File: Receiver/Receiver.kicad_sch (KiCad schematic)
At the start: 2 parts, among them J1 Conn_01x03, U1 TSSP4038

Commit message: gnd fills
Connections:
- net GND: now reaches J1.3 (Pin_3), U1.2
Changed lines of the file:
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@@
 	(generator_version "8.0")
 	(paper "A4")
+	(junction
+		(at 124.46 96.52)
+		(diameter 0)
+		(color 0 0 0 0)
+	)
 	(wire
 		(pts
@@
 					(unit 1)
 				)
+			)
+		)
+	)
+	(symbol
+		(lib_id "power:GND")
+		(at 124.46 96.52 0)
+		(unit 1)
+		(exclude_from_sim no)
+		(in_bom yes)
+		(on_board yes)
+		(dnp no)
+		(fields_autoplaced yes)
+		(property "Reference" "#PWR01"
+			(at 124.46 102.87 0)
+			(effects
+				(font
+					(size 1.27 1.27)
+				)
+				(hide yes)
+			)
+		)
+		(property "Value" "GND"
+			(at 124.46 101.6 0)
+			(effects
+				(font
+					(size 1.27 1.27)
+				)
+			)
+		)
+		(property "Footprint" ""
+			(at 124.46 96.52 0)
+			(effects
+				(font
+					(size 1.27 1.27)
+				)
+				(hide yes)
+			)
+		)
+		(property "Datasheet" ""
+			(at 124.46 96.52 0)
+			(effects
+				(font
+					(size 1.27 1.27)
+				)
+				(hide yes)
+			)
+		)
+		(property "Description" "Power symbol creates a global label with name \"GND\" , ground"
+			(at 124.46 96.52 0)
+			(effects
+				(font
+					(size 1.27 1.27)
+				)
+				(hide yes)
+			)
+		)
+		(pin "1"
+		)
+		(instances
+			(project "Receiver"
+				(path "/7e0fe819-ccc9-4312-883b-b9dcc40b4756"
+					(reference "#PWR01")
+					(unit 1)
+				)

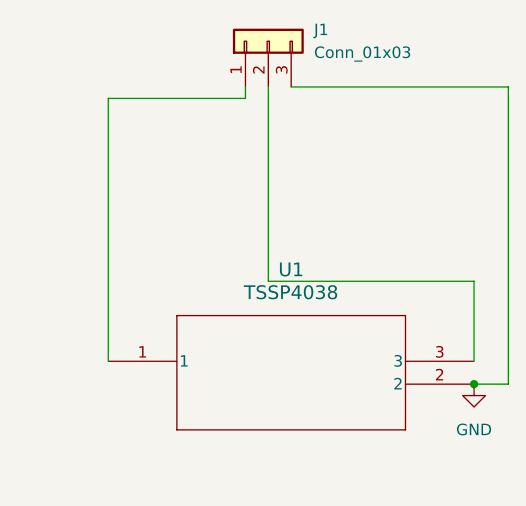
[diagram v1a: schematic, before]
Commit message: Added low pass filter to reciever pcb
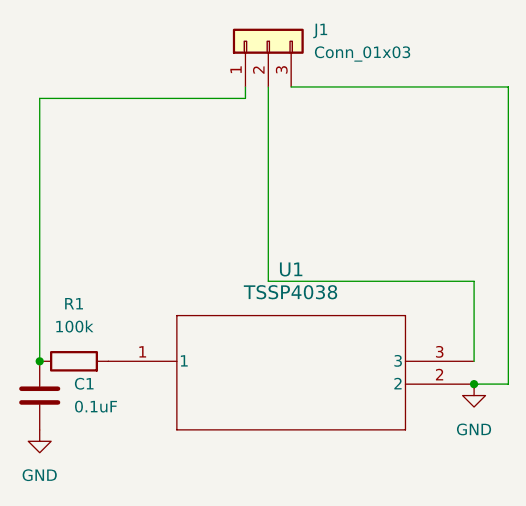
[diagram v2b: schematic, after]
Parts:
- added C1: 0.1uF, Capacitor_SMD:C_0805_2012Metric_Pad1.18x1.45mm_HandSolder, symbol Device:C
- added R1: 100k, Resistor_SMD:R_0805_2012Metric_Pad1.20x1.40mm_HandSolder, symbol Device:R
- J1: footprint Connector_JST:JST_XH_S3B-XH-A-1_1x03_P2.50mm_Horizontal -> Connector_JST:JST_XH_B3B-XH-AM_1x03_P2.50mm_Vertical
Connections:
- net GND: now also C1.2
- net at J1.1 (Pin_1): now also C1.1, R1.1; no longer U1.1
- new net: R1.2, U1.1
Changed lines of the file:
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@@
 	(paper "A4")
+	(junction
+		(at 76.2 93.98)
+		(diameter 0)
+		(color 0 0 0 0)
+	)
 	(junction
 		(at 124.46 96.52)
@@
 	(wire
 		(pts
-			(xy 83.82 64.77) (xy 83.82 93.98)
+			(xy 76.2 93.98) (xy 76.2 64.77)
 		)
 		(stroke
@@
 	(wire
 		(pts
-			(xy 99.06 64.77) (xy 83.82 64.77)
+			(xy 76.2 64.77) (xy 99.06 64.77)
 		)
 		(stroke
@@
 			)
 		)
-		(property "Footprint" "Connector_JST:JST_XH_S3B-XH-A-1_1x03_P2.50mm_Horizontal"
+		(property "Footprint" "Connector_JST:JST_XH_B3B-XH-AM_1x03_P2.50mm_Vertical"
 			(at 101.6 58.42 0)
 			(effects
@@
 	)
 	(symbol
+		(lib_id "Device:R")
+		(at 80.01 93.98 90)
+		(unit 1)
+		(exclude_from_sim no)
+		(in_bom yes)
+		(on_board yes)
+		(dnp no)
+		(fields_autoplaced yes)
+		(property "Reference" "R1"
+			(at 80.01 87.63 90)
+			(effects
+				(font
+					(size 1.27 1.27)
+				)
+			)
+		)
+		(property "Value" "100k"
+			(at 80.01 90.17 90)
+			(effects
+				(font
+					(size 1.27 1.27)
+				)
+			)
+		)
+		(property "Footprint" "Resistor_SMD:R_0805_2012Metric_Pad1.20x1.40mm_HandSolder"
+			(at 80.01 95.758 90)
+			(effects
+				(font
+					(size 1.27 1.27)
+				)
+				(hide yes)
+			)
+		)
+		(property "Datasheet" "~"
+			(at 80.01 93.98 0)
+			(effects
+				(font
+					(size 1.27 1.27)
+				)
+				(hide yes)
+			)
+		)
+		(property "Description" "Resistor"
+			(at 80.01 93.98 0)
+			(effects
+				(font
+					(size 1.27 1.27)
+				)
+				(hide yes)
+			)
+		)
+		(pin "2"
+		)
+		(pin "1"
+		)
+		(instances
+			(project "Receiver"
+				(path "/7e0fe819-ccc9-4312-883b-b9dcc40b4756"
+					(reference "R1")
+					(unit 1)
+				)
+			)
+		)
+	)
+	(symbol
 		(lib_id "2024-03-03_03-06-29:TSSP4038")
 		(at 83.82 93.98 0)
@@
 	(symbol
 		(lib_id "power:GND")
+		(at 76.2 101.6 0)
+		(unit 1)
+		(exclude_from_sim no)
+		(in_bom yes)
+		(on_board yes)
+		(dnp no)
+		(fields_autoplaced yes)
+		(property "Reference" "#PWR02"
+			(at 76.2 107.95 0)
+			(effects
+				(font
+					(size 1.27 1.27)
+				)
+				(hide yes)
+			)
+		)
+		(property "Value" "GND"
+			(at 76.2 106.68 0)
+			(effects
+				(font
+					(size 1.27 1.27)
+				)
+			)
+		)
+		(property "Footprint" ""
+			(at 76.2 101.6 0)
+			(effects
+				(font
+					(size 1.27 1.27)
+				)
+				(hide yes)
+			)
+		)
+		(property "Datasheet" ""
+			(at 76.2 101.6 0)
+			(effects
+				(font
+					(size 1.27 1.27)
+				)
+				(hide yes)
+			)
+		)
+		(property "Description" "Power symbol creates a global label with name \"GND\" , ground"
+			(at 76.2 101.6 0)
+			(effects
+				(font
+					(size 1.27 1.27)
+				)
+				(hide yes)
+			)
+		)
+		(pin "1"
+		)
+		(instances
+			(project "Receiver"
+				(path "/7e0fe819-ccc9-4312-883b-b9dcc40b4756"
+					(reference "#PWR02")
+					(unit 1)
+				)
+			)
+		)
+	)
+	(symbol
+		(lib_id "power:GND")
 		(at 124.46 96.52 0)
 		(unit 1)
@@
 					(unit 1)
 				)
+			)
+		)
+	)
+	(symbol
+		(lib_id "Device:C")
+		(at 76.2 97.79 0)
+		(unit 1)
+		(exclude_from_sim no)
+		(in_bom yes)
+		(on_board yes)
+		(dnp no)
+		(fields_autoplaced yes)
+		(property "Reference" "C1"
+			(at 80.01 96.5199 0)
+			(effects
+				(font
+					(size 1.27 1.27)
+				)
+				(justify left)
+			)
+		)
+		(property "Value" "0.1uF"
+			(at 80.01 99.0599 0)
+			(effects
+				(font
+					(size 1.27 1.27)
+				)
+				(justify left)
+			)
+		)
+		(property "Footprint" "Capacitor_SMD:C_0805_2012Metric_Pad1.18x1.45mm_HandSolder"
+			(at 77.1652 101.6 0)
+			(effects
+				(font
+					(size 1.27 1.27)
+				)
+				(hide yes)
+			)
+		)
+		(property "Datasheet" "~"
+			(at 76.2 97.79 0)
+			(effects
+				(font
+					(size 1.27 1.27)
+				)
+				(hide yes)
+			)
+		)
+		(property "Description" "Unpolarized capacitor"
+			(at 76.2 97.79 0)
+			(effects
+				(font
+					(size 1.27 1.27)
+				)
+				(hide yes)
+			)
+		)
+		(pin "2"
+		)
+		(pin "1"
+		)
+		(instances
+			(project "Receiver"
+				(path "/7e0fe819-ccc9-4312-883b-b9dcc40b4756"
+					(reference "C1")
+					(unit 1)
+				)
